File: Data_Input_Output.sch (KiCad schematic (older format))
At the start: 26 parts, among them P10 CONN_01X02, P11 CONN_01X02, P12 CONN_01X02, P3 CONN_01X04, P4 CONN_01X04, P5 CONN_01X04, P6 CONN_01X04, P7 CONN_01X02, P8 CONN_01X02, P9 CONN_01X02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

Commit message: small update
getting ready to order PCB's, making sure they are good to go.
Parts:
- removed P10, P11, P12: CONN_01X02, SPEX_Parts:ultraFitCONN_2, symbol CONN_01X02
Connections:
- net i2c_SCL_out: now also P3.2 (P2); no longer P3.3 (P3)
- net i2c_SDA_out: now also P3.3 (P3); no longer P3.2 (P2)
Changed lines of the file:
@@
 $EndDescr
 $Comp
-L GND #PWR70
+L GND #PWR064
 U 1 1 56EB177F
 P 5200 2550
-F 0 "#PWR70" H 5200 2300 50  0001 C CNN
+F 0 "#PWR064" H 5200 2300 50  0001 C CNN
 F 1 "GND" H 5200 2400 50  0000 C CNN
 F 2 "" H 5200 2550 60  0000 C CNN
@@
 Data_GND
 $Comp
-L +3.3V #PWR64
+L +3.3V #PWR065
 U 1 1 56EB1E10
 P 2450 950
-F 0 "#PWR64" H 2450 800 50  0001 C CNN
+F 0 "#PWR065" H 2450 800 50  0001 C CNN
 F 1 "+3.3V" H 2450 1090 50  0000 C CNN
 F 2 "" H 2450 950 60  0000 C CNN
@@
 $EndComp
 $Comp
-L GND #PWR65
+L GND #PWR066
 U 1 1 56EB1E33
 P 2450 1200
-F 0 "#PWR65" H 2450 950 50  0001 C CNN
+F 0 "#PWR066" H 2450 950 50  0001 C CNN
 F 1 "GND" H 2450 1050 50  0000 C CNN
 F 2 "" H 2450 1200 60  0000 C CNN
@@
 $EndComp
 $Comp
-L +3.3V #PWR66
+L +3.3V #PWR067
 U 1 1 56EB2146
 P 2550 2650
-F 0 "#PWR66" H 2550 2500 50  0001 C CNN
+F 0 "#PWR067" H 2550 2500 50  0001 C CNN
 F 1 "+3.3V" H 2550 2790 50  0000 C CNN
 F 2 "" H 2550 2650 60  0000 C CNN
@@
 $EndComp
 $Comp
-L GND #PWR67
+L GND #PWR068
 U 1 1 56EB216C
 P 2550 3950
-F 0 "#PWR67" H 2550 3700 50  0001 C CNN
+F 0 "#PWR068" H 2550 3700 50  0001 C CNN
 F 1 "GND" H 2550 3800 50  0000 C CNN
 F 2 "" H 2550 3950 60  0000 C CNN
@@
 SD_MISO
 $Comp
-L +3.3V #PWR69
+L +3.3V #PWR069
 U 1 1 56F427AD
 P 5150 1000
-F 0 "#PWR69" H 5150 850 50  0001 C CNN
+F 0 "#PWR069" H 5150 850 50  0001 C CNN
 F 1 "+3.3V" H 5150 1140 50  0000 C CNN
 F 2 "" H 5150 1000 60  0000 C CNN
@@
 $EndComp
 $Comp
-L +3.3V #PWR71
+L +3.3V #PWR070
 U 1 1 56F4344F
 P 5950 1600
-F 0 "#PWR71" H 5950 1450 50  0001 C CNN
+F 0 "#PWR070" H 5950 1450 50  0001 C CNN
 F 1 "+3.3V" H 5950 1740 50  0000 C CNN
 F 2 "" H 5950 1600 60  0000 C CNN
@@
 $EndComp
 $Comp
-L GND #PWR72
+L GND #PWR071
 U 1 1 56F43490
 P 5950 2400
-F 0 "#PWR72" H 5950 2150 50  0001 C CNN
+F 0 "#PWR071" H 5950 2150 50  0001 C CNN
 F 1 "GND" H 5950 2250 50  0000 C CNN
 F 2 "" H 5950 2400 60  0000 C CNN
@@
 SD_PWRCTRL
 $Comp
-L GND #PWR73
+L GND #PWR072
 U 1 1 56F6549F
 P 5950 3700
-F 0 "#PWR73" H 5950 3450 50  0001 C CNN
+F 0 "#PWR072" H 5950 3450 50  0001 C CNN
 F 1 "GND" H 5950 3550 50  0000 C CNN
 F 2 "" H 5950 3700 60  0000 C CNN
@@
 $EndComp
 $Comp
-L GND #PWR74
+L GND #PWR073
 U 1 1 56F66682
 P 5950 4650
-F 0 "#PWR74" H 5950 4400 50  0001 C CNN
+F 0 "#PWR073" H 5950 4400 50  0001 C CNN
 F 1 "GND" H 5950 4500 50  0000 C CNN
 F 2 "" H 5950 4650 60  0000 C CNN
@@
 $EndComp
 $Comp
-L GND #PWR75
+L GND #PWR074
 U 1 1 56F669B0
 P 5950 5600
-F 0 "#PWR75" H 5950 5350 50  0001 C CNN
+F 0 "#PWR074" H 5950 5350 50  0001 C CNN
 F 1 "GND" H 5950 5450 50  0000 C CNN
 F 2 "" H 5950 5600 60  0000 C CNN
@@
 	1    0    0    -1
 $EndComp
-$Comp
-L CONN_01X02 P10
-U 1 1 57037154
-P 10350 4950
-F 0 "P10" H 10350 5100 50  0000 C CNN
-F 1 "CONN_01X02" V 10450 4950 50  0000 C CNN
-F 2 "SPEX_Parts:ultraFitCONN_2" H 10350 4950 50  0001 C CNN
-F 3 "" H 10350 4950 50  0000 C CNN
-	1    10350 4950
-	1    0    0    -1
-$EndComp
-$Comp
-L CONN_01X02 P11
-U 1 1 570371E4
-P 10350 5450
-F 0 "P11" H 10350 5600 50  0000 C CNN
-F 1 "CONN_01X02" V 10450 5450 50  0000 C CNN
-F 2 "SPEX_Parts:ultraFitCONN_2" H 10350 5450 50  0001 C CNN
-F 3 "" H 10350 5450 50  0000 C CNN
-	1    10350 5450
-	1    0    0    -1
-$EndComp
 Wire Wire Line
 	10000 3500 10150 3500
-Wire Wire Line
-	10050 5500 10150 5500
 Wire Wire Line
 	9900 4500 10150 4500
@@
 Text HLabel 9900 4400 0    60   Input ~ 0
 Vbus_MOS_OUT
-Text HLabel 9900 4900 0    60   Input ~ 0
-Battery_Out
-Text HLabel 9900 5950 0    60   Input ~ 0
-User_Out
-$Comp
-L CONN_01X02 P12
-U 1 1 5703822A
-P 10350 6000
-F 0 "P12" H 10350 6150 50  0000 C CNN
-F 1 "CONN_01X02" V 10450 6000 50  0000 C CNN
-F 2 "SPEX_Parts:ultraFitCONN_2" H 10350 6000 50  0001 C CNN
-F 3 "" H 10350 6000 50  0000 C CNN
-	1    10350 6000
-	1    0    0    -1
-$EndComp
-Text HLabel 9900 5400 0    60   Input ~ 0
-User_In
-Wire Wire Line
-	10050 6050 10150 6050
-$Comp
-L GND #PWR86
+$Comp
+L GND #PWR075
 U 1 1 57038625
 P 10100 2600
-F 0 "#PWR86" H 10100 2350 50  0001 C CNN
+F 0 "#PWR075" H 10100 2350 50  0001 C CNN
 F 1 "GND" H 10100 2450 50  0000 C CNN
 F 2 "" H 10100 2600 60  0000 C CNN
@@
 $EndComp
 $Comp
-L GND #PWR84
+L GND #PWR076
 U 1 1 5703869C
 P 10100 1700
-F 0 "#PWR84" H 10100 1450 50  0001 C CNN
+F 0 "#PWR076" H 10100 1450 50  0001 C CNN
 F 1 "GND" H 10100 1550 50  0000 C CNN
 F 2 "" H 10100 1700 60  0000 C CNN
@@
 	10100 2500 10100 2600
 $Comp
-L +3.3V #PWR83
+L +3.3V #PWR077
 U 1 1 57038AFB
 P 10100 1200
-F 0 "#PWR83" H 10100 1050 50  0001 C CNN
+F 0 "#PWR077" H 10100 1050 50  0001 C CNN
 F 1 "+3.3V" H 10100 1340 50  0000 C CNN
 F 2 "" H 10100 1200 60  0000 C CNN
@@
 $EndComp
 $Comp
-L +3.3V #PWR85
+L +3.3V #PWR078
 U 1 1 57038B72
 P 10100 2100
-F 0 "#PWR85" H 10100 1950 50  0001 C CNN
+F 0 "#PWR078" H 10100 1950 50  0001 C CNN
 F 1 "+3.3V" H 10100 2240 50  0000 C CNN
 F 2 "" H 10100 2100 60  0000 C CNN
@@
 Wire Wire Line
 	10150 4400 9900 4400
-Wire Wire Line
-	10150 4900 9900 4900
-Wire Wire Line
-	10150 5400 9900 5400
-Wire Wire Line
-	10150 5950 9900 5950
 $Comp
 L CONN_01X04 P3
@@
 $EndComp
 $Comp
-L +3.3V #PWR76
+L +3.3V #PWR079
 U 1 1 57039D7A
 P 8750 1200
-F 0 "#PWR76" H 8750 1050 50  0001 C CNN
+F 0 "#PWR079" H 8750 1050 50  0001 C CNN
 F 1 "+3.3V" H 8750 1340 50  0000 C CNN
 F 2 "" H 8750 1200 60  0000 C CNN
@@
 $EndComp
 $Comp
-L GND #PWR77
+L GND #PWR080
 U 1 1 57039E1D
 P 8750 1700
-F 0 "#PWR77" H 8750 1450 50  0001 C CNN
+F 0 "#PWR080" H 8750 1450 50  0001 C CNN
 F 1 "GND" H 8750 1550 50  0000 C CNN
 F 2 "" H 8750 1700 60  0000 C CNN
@@
 Wire Wire Line
 	8750 1300 8750 1200
+Text HLabel 8550 1500 0    60   Input ~ 0
+i2c_SDA_out
 Text HLabel 8550 1400 0    60   Input ~ 0
-i2c_SDA_out
-Text HLabel 8550 1500 0    60   Input ~ 0
 i2c_SCL_out
 Wire Wire Line
@@
 $EndComp
 $Comp
-L +3.3V #PWR78
+L +3.3V #PWR081
 U 1 1 57033FCB
 P 8750 2100
-F 0 "#PWR78" H 8750 1950 50  0001 C CNN
+F 0 "#PWR081" H 8750 1950 50  0001 C CNN
 F 1 "+3.3V" H 8750 2240 50  0000 C CNN
 F 2 "" H 8750 2100 60  0000 C CNN
@@
 $EndComp
 $Comp
-L GND #PWR79
+L GND #PWR082
 U 1 1 57033FD1
 P 8750 2600
-F 0 "#PWR79" H 8750 2350 50  0001 C CNN
+F 0 "#PWR082" H 8750 2350 50  0001 C CNN
 F 1 "GND" H 8750 2450 50  0000 C CNN
 F 2 "" H 8750 2600 60  0000 C CNN
@@
 UART_RX_out
 $Comp
-L +3.3V #PWR80
+L +3.3V #PWR083
 U 1 1 570406FF
 P 10000 3300
-F 0 "#PWR80" H 10000 3150 50  0001 C CNN
+F 0 "#PWR083" H 10000 3150 50  0001 C CNN
 F 1 "+3.3V" H 10000 3440 50  0000 C CNN
 F 2 "" H 10000 3300 60  0000 C CNN
@@
 	10000 3300 10000 3500
 $Comp
-L +5V #PWR81
+L +5V #PWR084
 U 1 1 57040BC0
 P 10000 3800
-F 0 "#PWR81" H 10000 3650 50  0001 C CNN
+F 0 "#PWR084" H 10000 3650 50  0001 C CNN
 F 1 "+5V" H 10000 3940 50  0000 C CNN
 F 2 "" H 10000 3800 50  0000 C CNN
@@
 5V_in
 $Comp
-L +5V #PWR68
+L +5V #PWR085
 U 1 1 57044D2C
 P 2700 950
-F 0 "#PWR68" H 2700 800 50  0001 C CNN
+F 0 "#PWR085" H 2700 800 50  0001 C CNN
 F 1 "+5V" H 2700 1090 50  0000 C CNN
 F 2 "" H 2700 950 50  0000 C CNN
@@
 Wire Wire Line
 	2700 1000 2900 1000
-$Comp
-L GND #PWR82
-U 1 1 57047398
-P 10050 6150
-F 0 "#PWR82" H 10050 5900 50  0001 C CNN
-F 1 "GND" H 10050 6000 50  0000 C CNN
-F 2 "" H 10050 6150 60  0000 C CNN
-F 3 "" H 10050 6150 60  0000 C CNN
-	1    10050 6150
-	1    0    0    -1
-$EndComp
-Wire Wire Line
-	10050 5000 10050 6150
-Connection ~ 10050 6050
-Wire Wire Line
-	10050 5000 10150 5000
-Connection ~ 10050 5500
 Text HLabel 9750 2400 0    60   Input ~ 0
 I/O2

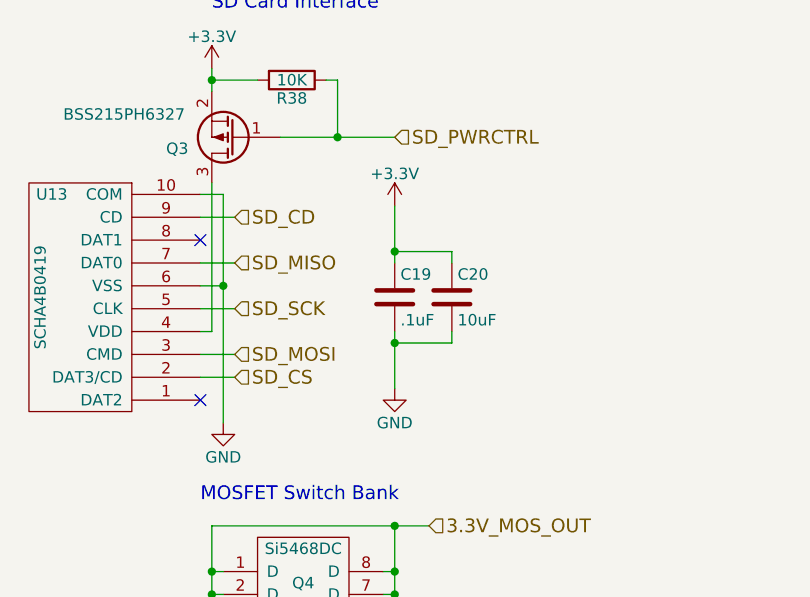
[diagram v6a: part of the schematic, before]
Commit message: small update round 2
cleaning up PCB, adding SPI CS pullup resistors
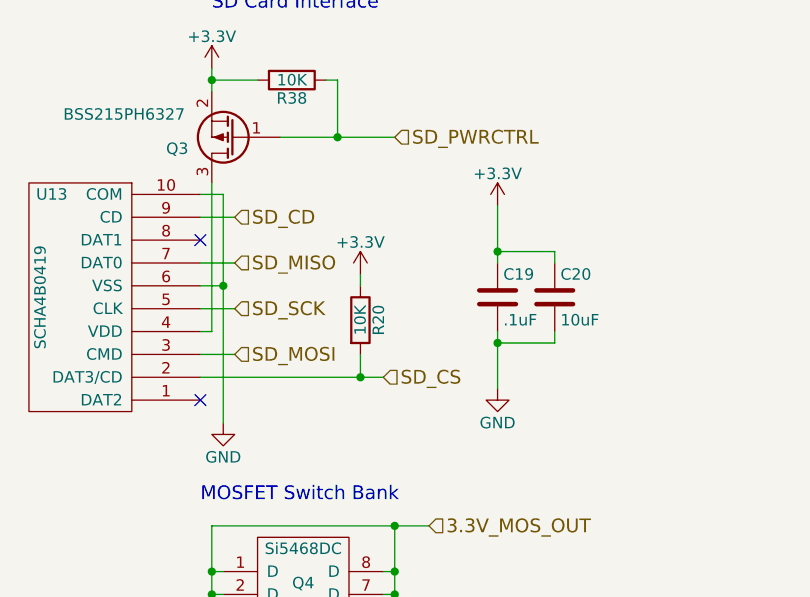
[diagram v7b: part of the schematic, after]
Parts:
- added R20: 10K, Resistors_SMD:R_0603, symbol R
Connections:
- net +3V3: now also R20.1
- net SD_CS: now also R20.2
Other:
- moved on the sheet: C19, C20
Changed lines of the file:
@@
 Text Notes 9300 900  0    60   ~ 0
 Headers\n
-Text HLabel 5250 2350 2    60   Input ~ 0
+Text HLabel 5900 2350 2    60   Input ~ 0
 SD_CS
 Text HLabel 5250 2250 2    60   Input ~ 0
@@
 L C C19
 U 1 1 56F4339B
-P 5950 2000
-F 0 "C19" H 5975 2100 50  0000 L CNN
-F 1 ".1uF" H 5975 1900 50  0000 L CNN
-F 2 "Capacitors_SMD:C_0603" H 5988 1850 50  0001 C CNN
-F 3 "" H 5950 2000 50  0000 C CNN
-	1    5950 2000
+P 6400 2000
+F 0 "C19" H 6425 2100 50  0000 L CNN
+F 1 ".1uF" H 6425 1900 50  0000 L CNN
+F 2 "Capacitors_SMD:C_0603" H 6438 1850 50  0001 C CNN
+F 3 "" H 6400 2000 50  0000 C CNN
+	1    6400 2000
 	1    0    0    -1
 $EndComp
@@
 L C C20
 U 1 1 56F433E0
-P 6200 2000
-F 0 "C20" H 6225 2100 50  0000 L CNN
-F 1 "10uF" H 6225 1900 50  0000 L CNN
-F 2 "Capacitors_SMD:C_0603" H 6238 1850 50  0001 C CNN
-F 3 "" H 6200 2000 50  0000 C CNN
-	1    6200 2000
+P 6650 2000
+F 0 "C20" H 6675 2100 50  0000 L CNN
+F 1 "10uF" H 6675 1900 50  0000 L CNN
+F 2 "Capacitors_SMD:C_0603" H 6688 1850 50  0001 C CNN
+F 3 "" H 6650 2000 50  0000 C CNN
+	1    6650 2000
 	1    0    0    -1
 $EndComp
@@
 L +3.3V #PWR070
 U 1 1 56F4344F
-P 5950 1600
-F 0 "#PWR070" H 5950 1450 50  0001 C CNN
-F 1 "+3.3V" H 5950 1740 50  0000 C CNN
-F 2 "" H 5950 1600 60  0000 C CNN
-F 3 "" H 5950 1600 60  0000 C CNN
-	1    5950 1600
+P 6400 1600
+F 0 "#PWR070" H 6400 1450 50  0001 C CNN
+F 1 "+3.3V" H 6400 1740 50  0000 C CNN
+F 2 "" H 6400 1600 60  0000 C CNN
+F 3 "" H 6400 1600 60  0000 C CNN
+	1    6400 1600
 	1    0    0    -1
 $EndComp
@@
 L GND #PWR071
 U 1 1 56F43490
-P 5950 2400
-F 0 "#PWR071" H 5950 2150 50  0001 C CNN
-F 1 "GND" H 5950 2250 50  0000 C CNN
-F 2 "" H 5950 2400 60  0000 C CNN
-F 3 "" H 5950 2400 60  0000 C CNN
-	1    5950 2400
+P 6400 2400
+F 0 "#PWR071" H 6400 2150 50  0001 C CNN
+F 1 "GND" H 6400 2250 50  0000 C CNN
+F 2 "" H 6400 2400 60  0000 C CNN
+F 3 "" H 6400 2400 60  0000 C CNN
+	1    6400 2400
 	1    0    0    -1
 $EndComp
@@
 Connection ~ 2400 3150
 Wire Wire Line
-	5250 2350 5100 2350
+	5100 2350 5900 2350
 Wire Wire Line
 	5250 1850 5100 1850
@@
 	5250 1650 5100 1650
 Wire Wire Line
-	5950 2150 5950 2400
-Wire Wire Line
-	6200 2150 6200 2200
-Wire Wire Line
-	6200 2200 5950 2200
-Connection ~ 5950 2200
-Wire Wire Line
-	5950 1600 5950 1850
-Wire Wire Line
-	6200 1850 6200 1800
-Wire Wire Line
-	6200 1800 5950 1800
-Connection ~ 5950 1800
+	6400 2150 6400 2400
+Wire Wire Line
+	6650 2150 6650 2200
+Wire Wire Line
+	6650 2200 6400 2200
+Connection ~ 6400 2200
+Wire Wire Line
+	6400 1600 6400 1850
+Wire Wire Line
+	6650 1850 6650 1800
+Wire Wire Line
+	6650 1800 6400 1800
+Connection ~ 6400 1800
 Wire Wire Line
 	5150 1000 5150 1100
@@
 Text HLabel 9750 2300 0    60   Input ~ 0
 I/O1
+$Comp
+L R R20
+U 1 1 580822D7
+P 5800 2100
+F 0 "R20" V 5880 2100 50  0000 C CNN
+F 1 "10K" V 5800 2100 50  0000 C CNN
+F 2 "Resistors_SMD:R_0603" V 5730 2100 50  0001 C CNN
+F 3 "" H 5800 2100 50  0000 C CNN
+	1    5800 2100
+	1    0    0    -1
+$EndComp
+Wire Wire Line
+	5800 2350 5800 2250
+Connection ~ 5800 2350
+$Comp
+L +3.3V #PWR086
+U 1 1 580825C1
+P 5800 1900
+F 0 "#PWR086" H 5800 1750 50  0001 C CNN
+F 1 "+3.3V" H 5800 2040 50  0000 C CNN
+F 2 "" H 5800 1900 60  0000 C CNN
+F 3 "" H 5800 1900 60  0000 C CNN
+	1    5800 1900
+	1    0    0    -1
+$EndComp
+Wire Wire Line
+	5800 1900 5800 1950
 $EndSCHEMATC

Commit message: small tweaks, BOM updated
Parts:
- added R21, R22: 50K, Resistors_SMD:R_0603, symbol R
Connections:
- net +3V3: now also R21.1, R22.2
- net at U13.1 (DAT2): now also R22.1
- net at U13.8 (DAT1): now also R21.2
- no-connect marks 2 -> 0
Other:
- moved on the sheet: C19, C20, R20
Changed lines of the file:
@@
 LIBS:valves
 LIBS:parts
-LIBS:PRESSURE-BMP180_LGA7_
 LIBS:74xgxx
 LIBS:ac-dc
@@
 Text Notes 9300 900  0    60   ~ 0
 Headers\n
-Text HLabel 5900 2350 2    60   Input ~ 0
+Text HLabel 6400 2350 2    60   Input ~ 0
 SD_CS
 Text HLabel 5250 2250 2    60   Input ~ 0
@@
 	1    0    0    -1
 $EndComp
-NoConn ~ 5100 2450
-NoConn ~ 5100 1750
 Text HLabel 5250 1650 2    60   Input ~ 0
 SD_CD
@@
 L C C19
 U 1 1 56F4339B
-P 6400 2000
-F 0 "C19" H 6425 2100 50  0000 L CNN
-F 1 ".1uF" H 6425 1900 50  0000 L CNN
-F 2 "Capacitors_SMD:C_0603" H 6438 1850 50  0001 C CNN
-F 3 "" H 6400 2000 50  0000 C CNN
-	1    6400 2000
+P 6900 2000
+F 0 "C19" H 6925 2100 50  0000 L CNN
+F 1 ".1uF" H 6925 1900 50  0000 L CNN
+F 2 "Capacitors_SMD:C_0603" H 6938 1850 50  0001 C CNN
+F 3 "" H 6900 2000 50  0000 C CNN
+	1    6900 2000
 	1    0    0    -1
 $EndComp
@@
 L C C20
 U 1 1 56F433E0
-P 6650 2000
-F 0 "C20" H 6675 2100 50  0000 L CNN
-F 1 "10uF" H 6675 1900 50  0000 L CNN
-F 2 "Capacitors_SMD:C_0603" H 6688 1850 50  0001 C CNN
-F 3 "" H 6650 2000 50  0000 C CNN
-	1    6650 2000
+P 7150 2000
+F 0 "C20" H 7175 2100 50  0000 L CNN
+F 1 "10uF" H 7175 1900 50  0000 L CNN
+F 2 "Capacitors_SMD:C_0603" H 7188 1850 50  0001 C CNN
+F 3 "" H 7150 2000 50  0000 C CNN
+	1    7150 2000
 	1    0    0    -1
 $EndComp
@@
 L +3.3V #PWR070
 U 1 1 56F4344F
-P 6400 1600
-F 0 "#PWR070" H 6400 1450 50  0001 C CNN
-F 1 "+3.3V" H 6400 1740 50  0000 C CNN
-F 2 "" H 6400 1600 60  0000 C CNN
-F 3 "" H 6400 1600 60  0000 C CNN
-	1    6400 1600
+P 6900 1600
+F 0 "#PWR070" H 6900 1450 50  0001 C CNN
+F 1 "+3.3V" H 6900 1740 50  0000 C CNN
+F 2 "" H 6900 1600 60  0000 C CNN
+F 3 "" H 6900 1600 60  0000 C CNN
+	1    6900 1600
 	1    0    0    -1
 $EndComp
@@
 L GND #PWR071
 U 1 1 56F43490
-P 6400 2400
-F 0 "#PWR071" H 6400 2150 50  0001 C CNN
-F 1 "GND" H 6400 2250 50  0000 C CNN
-F 2 "" H 6400 2400 60  0000 C CNN
-F 3 "" H 6400 2400 60  0000 C CNN
-	1    6400 2400
+P 6900 2400
+F 0 "#PWR071" H 6900 2150 50  0001 C CNN
+F 1 "GND" H 6900 2250 50  0000 C CNN
+F 2 "" H 6900 2400 60  0000 C CNN
+F 3 "" H 6900 2400 60  0000 C CNN
+	1    6900 2400
 	1    0    0    -1
 $EndComp
@@
 Connection ~ 2400 3150
 Wire Wire Line
-	5100 2350 5900 2350
+	5100 2350 6400 2350
 Wire Wire Line
 	5250 1850 5100 1850
@@
 	5250 1650 5100 1650
 Wire Wire Line
-	6400 2150 6400 2400
-Wire Wire Line
-	6650 2150 6650 2200
-Wire Wire Line
-	6650 2200 6400 2200
-Connection ~ 6400 2200
-Wire Wire Line
-	6400 1600 6400 1850
-Wire Wire Line
-	6650 1850 6650 1800
-Wire Wire Line
-	6650 1800 6400 1800
-Connection ~ 6400 1800
+	6900 2150 6900 2400
+Wire Wire Line
+	7150 2150 7150 2200
+Wire Wire Line
+	7150 2200 6900 2200
+Connection ~ 6900 2200
+Wire Wire Line
+	6900 1600 6900 1850
+Wire Wire Line
+	7150 1850 7150 1800
+Wire Wire Line
+	7150 1800 6900 1800
+Connection ~ 6900 1800
 Wire Wire Line
 	5150 1000 5150 1100
@@
 L R R20
 U 1 1 580822D7
-P 5800 2100
-F 0 "R20" V 5880 2100 50  0000 C CNN
-F 1 "10K" V 5800 2100 50  0000 C CNN
-F 2 "Resistors_SMD:R_0603" V 5730 2100 50  0001 C CNN
-F 3 "" H 5800 2100 50  0000 C CNN
-	1    5800 2100
-	1    0    0    -1
-$EndComp
-Wire Wire Line
-	5800 2350 5800 2250
-Connection ~ 5800 2350
+P 6300 2100
+F 0 "R20" V 6380 2100 50  0000 C CNN
+F 1 "10K" V 6300 2100 50  0000 C CNN
+F 2 "Resistors_SMD:R_0603" V 6230 2100 50  0001 C CNN
+F 3 "" H 6300 2100 50  0000 C CNN
+	1    6300 2100
+	1    0    0    -1
+$EndComp
+Wire Wire Line
+	6300 2350 6300 2250
+Connection ~ 6300 2350
 $Comp
 L +3.3V #PWR086
 U 1 1 580825C1
-P 5800 1900
-F 0 "#PWR086" H 5800 1750 50  0001 C CNN
-F 1 "+3.3V" H 5800 2040 50  0000 C CNN
-F 2 "" H 5800 1900 60  0000 C CNN
-F 3 "" H 5800 1900 60  0000 C CNN
-	1    5800 1900
-	1    0    0    -1
-$EndComp
-Wire Wire Line
-	5800 1900 5800 1950
+P 6300 1600
+F 0 "#PWR086" H 6300 1450 50  0001 C CNN
+F 1 "+3.3V" H 6300 1740 50  0000 C CNN
+F 2 "" H 6300 1600 60  0000 C CNN
+F 3 "" H 6300 1600 60  0000 C CNN
+	1    6300 1600
+	1    0    0    -1
+$EndComp
+Wire Wire Line
+	6300 1600 6300 1950
+$Comp
+L R R21
+U 1 1 58593134
+P 5950 1750
+F 0 "R21" V 6030 1750 50  0000 C CNN
+F 1 "50K" V 5950 1750 50  0000 C CNN
+F 2 "Resistors_SMD:R_0603" V 5880 1750 50  0001 C CNN
+F 3 "" H 5950 1750 50  0000 C CNN
+	1    5950 1750
+	0    1    1    0
+$EndComp
+$Comp
+L R R22
+U 1 1 585931D8
+P 5950 2450
+F 0 "R22" V 5850 2450 50  0000 C CNN
+F 1 "50K" V 5950 2450 50  0000 C CNN
+F 2 "Resistors_SMD:R_0603" V 5880 2450 50  0001 C CNN
+F 3 "" H 5950 2450 50  0000 C CNN
+	1    5950 2450
+	0    -1   -1   0
+$EndComp
+Wire Wire Line
+	5800 2450 5100 2450
+Wire Wire Line
+	6100 2450 6150 2450
+Wire Wire Line
+	6150 2450 6150 1750
+Wire Wire Line
+	6100 1750 6300 1750
+Connection ~ 6150 1750
+Connection ~ 6300 1750
+Wire Wire Line
+	5800 1750 5100 1750
 $EndSCHEMATC
